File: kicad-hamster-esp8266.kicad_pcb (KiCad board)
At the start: 2 copper layers, 35 parts, among them J1 Power Supply, J2 UART, J3 Screw_Terminal_01x02, J4 Screw_Terminal_01x02, J5 Screw_Terminal_01x02, J6 Screw_Terminal_01x02, Q1 IRLML5203, SW1 Reset, SW2 Flash, U1 ADM706P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

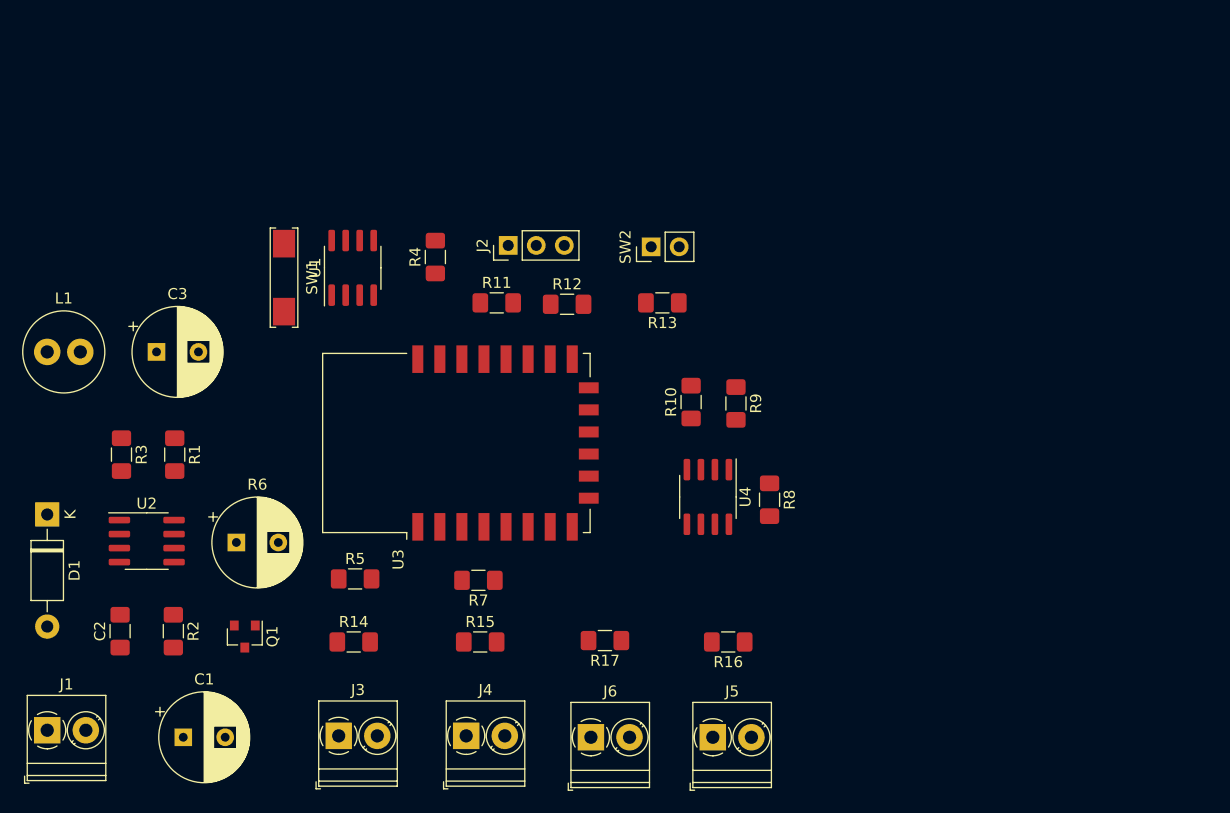
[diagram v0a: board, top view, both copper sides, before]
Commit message: pcb: first layout version
Signed-off-by: Sergey Matyukevich <geomatsi@gmail.com>
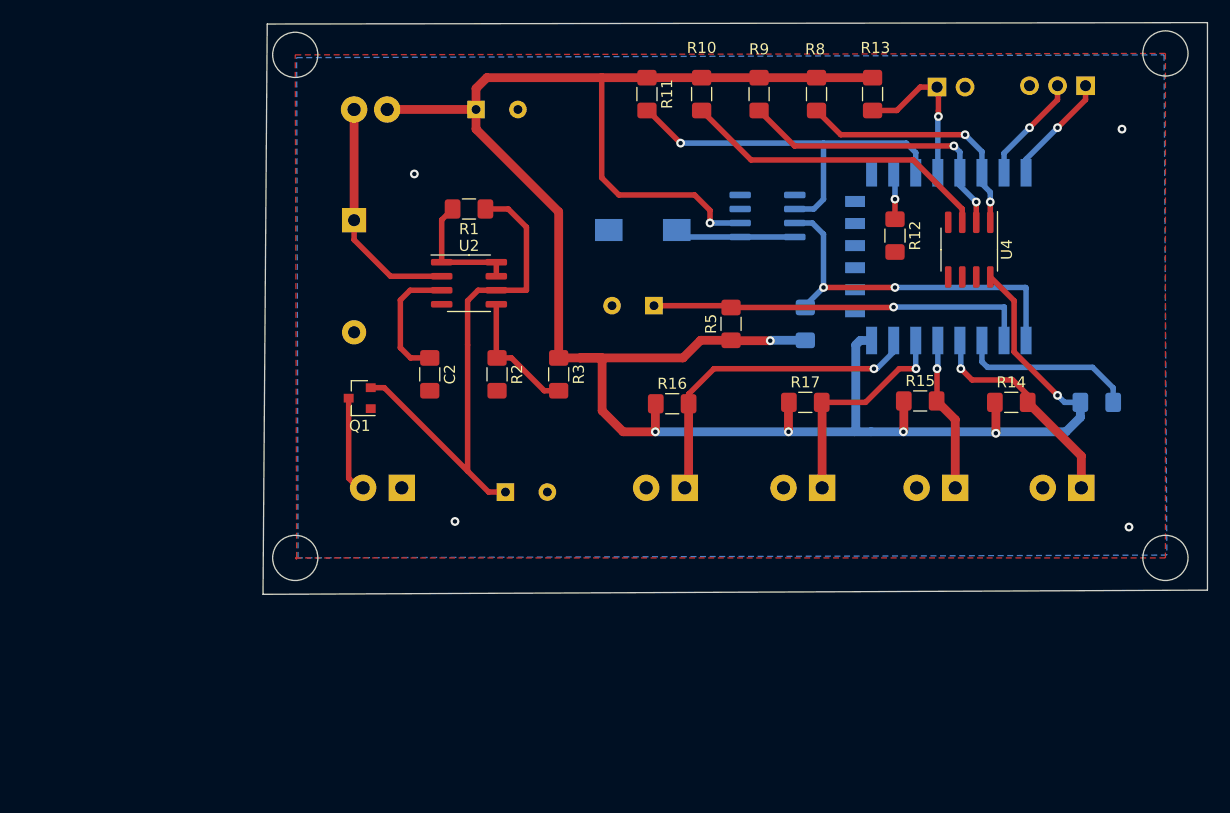
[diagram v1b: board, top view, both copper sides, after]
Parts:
- C1, C3, D1, J1, J2, J3, J4, J5, J6, L1, R4, R6, R7, SW1, SW2, U1, U3: moved to B.Cu
- moved J3 71.0 mm to (184.3, 96.6), turned to 180 degrees
- moved R14 63.4 mm to (177.9, 88.9)
- moved R7 58.3 mm to (185.7, 88.9), turned to 0 degrees
- moved J2 54.3 mm to (184.7, 60.2)
- moved U3 51.0 mm to (175.8, 75.7)
- moved J4 49.7 mm to (172.8, 96.6), turned to 180 degrees
- moved R15 45.5 mm to (169.7, 88.8)
- moved R6 43.5 mm to (145.5, 80.1), turned to 180 degrees
- moved R5 41.2 mm to (152.5, 81.8), turned to 90 degrees
- moved R3 40.3 mm to (136.9, 86.4)
- moved J1 38.9 mm to (122.7, 96.6), turned to 180 degrees
- moved D1 38.5 mm to (118.4, 72.4)
- moved U1 37.9 mm to (155.8, 72.0), turned to 0 degrees
- moved R2 37.4 mm to (131.3, 86.4)
- moved U2 37.4 mm to (128.8, 78.1)
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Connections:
- U3 pad 19: Net-(R8-Pad1) -> Net-(R9-Pad2)
- U3 pad 20: Net-(R9-Pad2) -> Net-(R8-Pad1)
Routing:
- net +3V3: track 0.00 -> 207.9 mm, vias 0 -> 7
- net Net-(C1-Pad1): track 0.00 -> 47.4 mm
- net Net-(R11-Pad2): track 0.00 -> 35.8 mm, vias 0 -> 1
- net Net-(R5-Pad2): track 0.00 -> 34.9 mm, vias 0 -> 1
- net Net-(R4-Pad2): track 0.00 -> 33.5 mm, vias 0 -> 2
- net Net-(J5-Pad1): track 0.00 -> 29.9 mm, vias 0 -> 1
- net Net-(R10-Pad1): track 0.00 -> 28.5 mm
- net Net-(R9-Pad2): track 0.00 -> 26.7 mm, vias 0 -> 2
- net Net-(R8-Pad1): track 0.00 -> 23.3 mm, vias 0 -> 2
- net Net-(D1-Pad1): track 0.00 -> 21.1 mm
- net Net-(J6-Pad1): track 0.00 -> 20.1 mm, vias 0 -> 1
- net Net-(J3-Pad1): track 0.00 -> 20.1 mm, vias 0 -> 1
- net Net-(R7-Pad2): track 0.00 -> 16.1 mm
- net Net-(R13-Pad2): track 0.00 -> 14.6 mm, vias 0 -> 1
- net Net-(J4-Pad1): track 0.00 -> 14.1 mm, vias 0 -> 1
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- added copper zone on B.Cu, net GND
- added copper zone on F.Cu, net GND
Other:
- board outline added: 85.6 x 51.8 mm
- net class medium added: clearance 0.2, trace_width 0.5, via_dia 0.8, via_drill 0.4

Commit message: pcb: text and updated footprint
- modify footprint of reed switch connector
- add silkscreen text

Signed-off-by: Sergey Matyukevich <geomatsi@gmail.com>
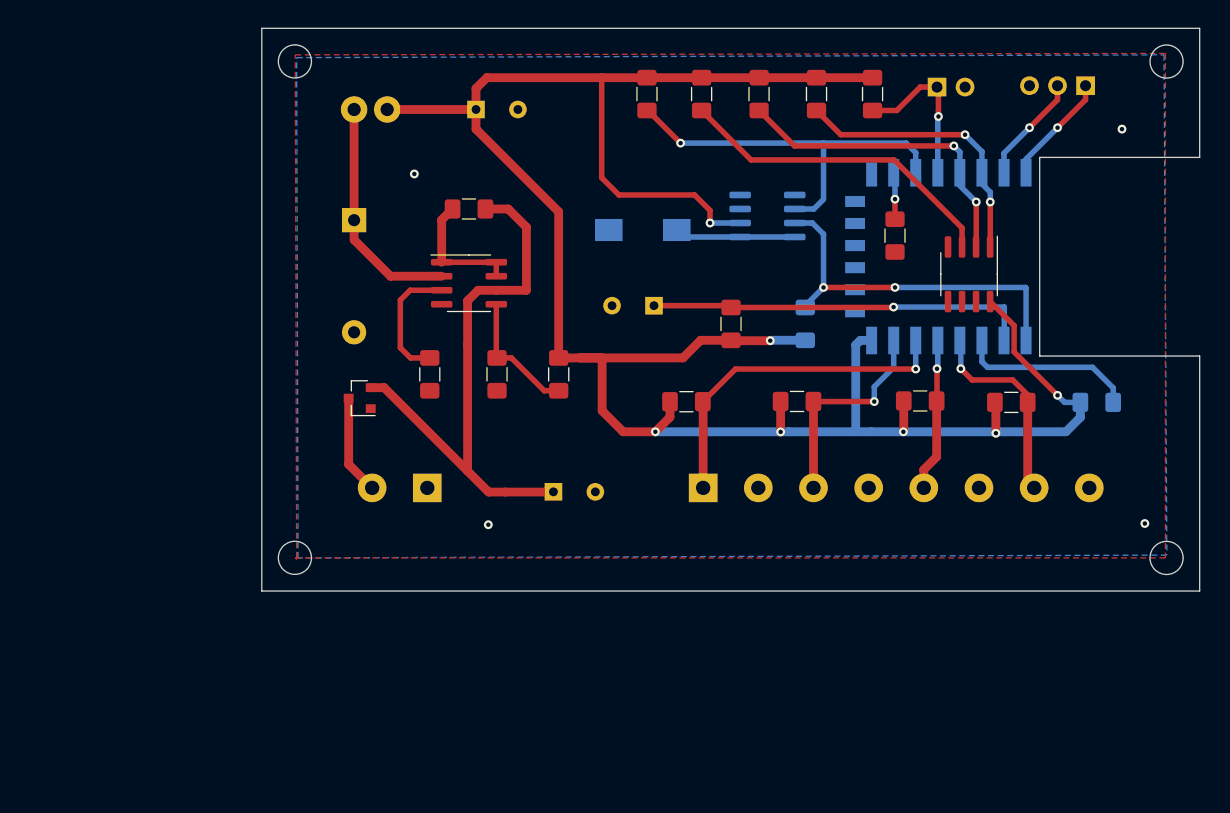
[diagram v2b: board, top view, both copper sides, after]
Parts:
- removed J4, J5, J6: Screw_Terminal_01x02, TerminalBlock_Phoenix:TerminalBlock_Phoenix_PT-1,5-2-3.5-H_1x02_P3.50mm_Horizontal
- J1: footprint TerminalBlock_Phoenix:TerminalBlock_Phoenix_PT-1,5-2-3.5-H_1x02_P3.50mm_Horizontal -> TerminalBlock_Phoenix:TerminalBlock_Phoenix_MKDS-1,5-2_1x02_P5.00mm_Horizontal
- J3: value Screw_Terminal_01x02 -> Screw_Terminal_01x08; footprint TerminalBlock_Phoenix:TerminalBlock_Phoenix_PT-1,5-2-3.5-H_1x02_P3.50mm_Horizontal -> TerminalBlock_Phoenix:TerminalBlock_Phoenix_MKDS-1,5-8_1x08_P5.00mm_Horizontal
- moved J3 34.3 mm to (150.0, 96.7), turned to 0 degrees
- moved R16 11.3 mm to (158.5, 88.8)
- moved R17 10.8 mm to (148.5, 88.8)
- moved C1 4.35 mm to (136.4, 97.0)
- moved J1 2.32 mm to (125.0, 96.7)
- moved U4 2.23 mm to (174.1, 77.3)
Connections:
- R14 pad 2: Net-(J3-Pad1) -> Net-(J3-Pad7)
- R15 pad 2: Net-(J4-Pad1) -> Net-(J3-Pad5)
- R16 pad 2: Net-(J5-Pad1) -> Net-(J3-Pad3)
- R17 pad 2: Net-(J6-Pad1) -> Net-(J3-Pad1)
- U3 pad 4: Net-(J3-Pad1) -> Net-(J3-Pad7)
- U3 pad 5: Net-(J4-Pad1) -> Net-(J3-Pad5)
- U3 pad 6: Net-(J6-Pad1) -> Net-(J3-Pad1)
- U3 pad 7: Net-(J5-Pad1) -> Net-(J3-Pad3)
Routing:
- net Net-(J5-Pad1): track 29.9 -> 0.00 mm, vias 1 -> 0
- net Net-(J6-Pad1): track 20.1 -> 0.00 mm, vias 1 -> 0
- net Net-(J3-Pad3): track 0.00 -> 19.6 mm, vias 0 -> 1
- net Net-(J3-Pad7): track 0.00 -> 18.3 mm, vias 0 -> 1
- net Net-(J4-Pad1): track 14.1 -> 0.00 mm, vias 1 -> 0
- net Net-(J3-Pad5): track 0.00 -> 13.9 mm, vias 0 -> 1
- net Net-(J3-Pad1): track 20.1 -> 30.9 mm
- net Net-(C1-Pad1): track 47.4 -> 51.8 mm
- net Net-(R9-Pad2): track 26.7 -> 29.0 mm
- net Net-(R8-Pad1): track 23.3 -> 25.5 mm
- net +3V3: track 207.9 -> 206.5 mm
- net Net-(R10-Pad1): track 28.5 -> 29.7 mm
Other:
- board size 85.6 x 51.8 mm -> 85 x 51 mm
- board text added: "- +"
- board text added: "FLASH"
- board text added: "Hamster v2.0"
- board text added: "RESET"
- board text added: "RX TX GND"
